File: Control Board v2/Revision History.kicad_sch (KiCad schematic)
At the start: 0 parts

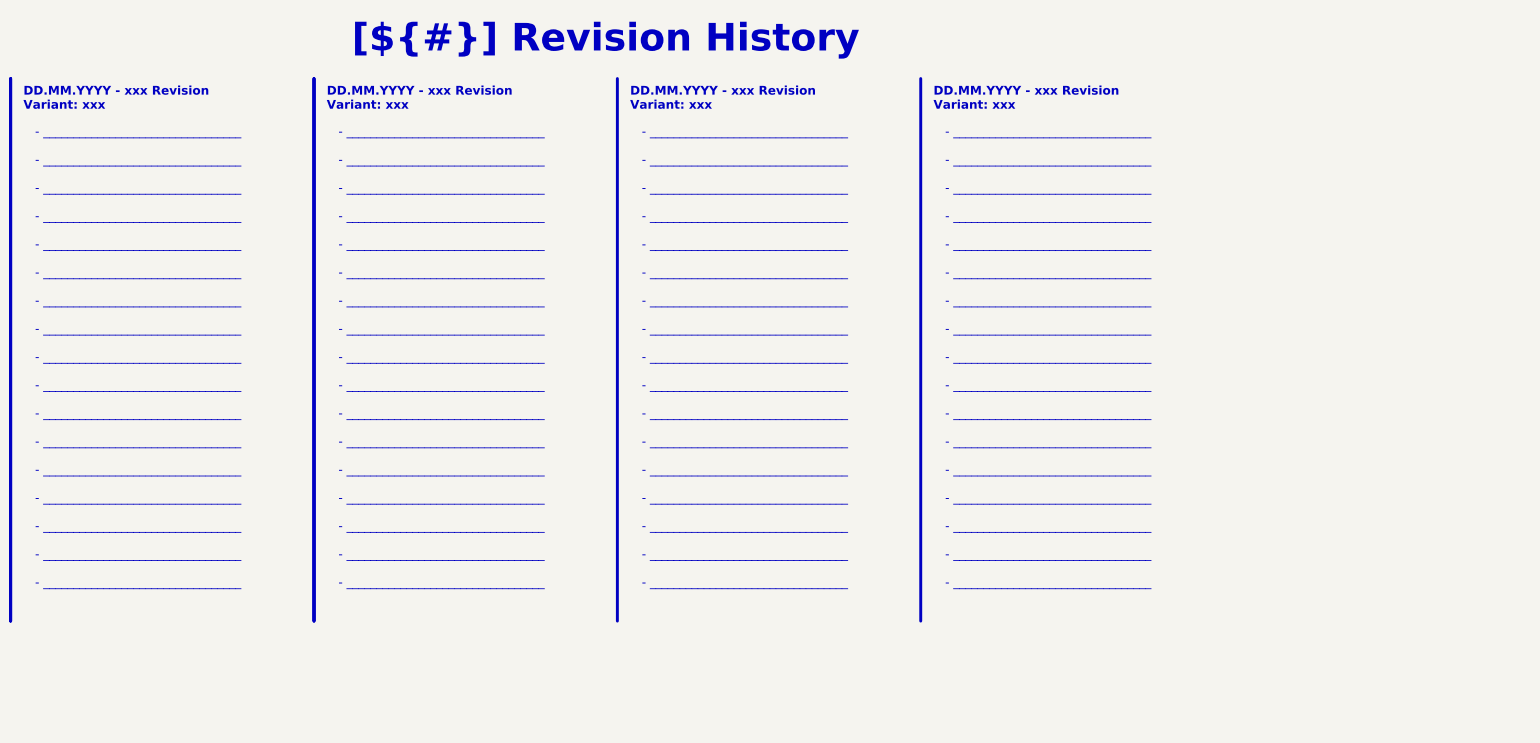
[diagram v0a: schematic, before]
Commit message: Finish preparing the template for v2 design
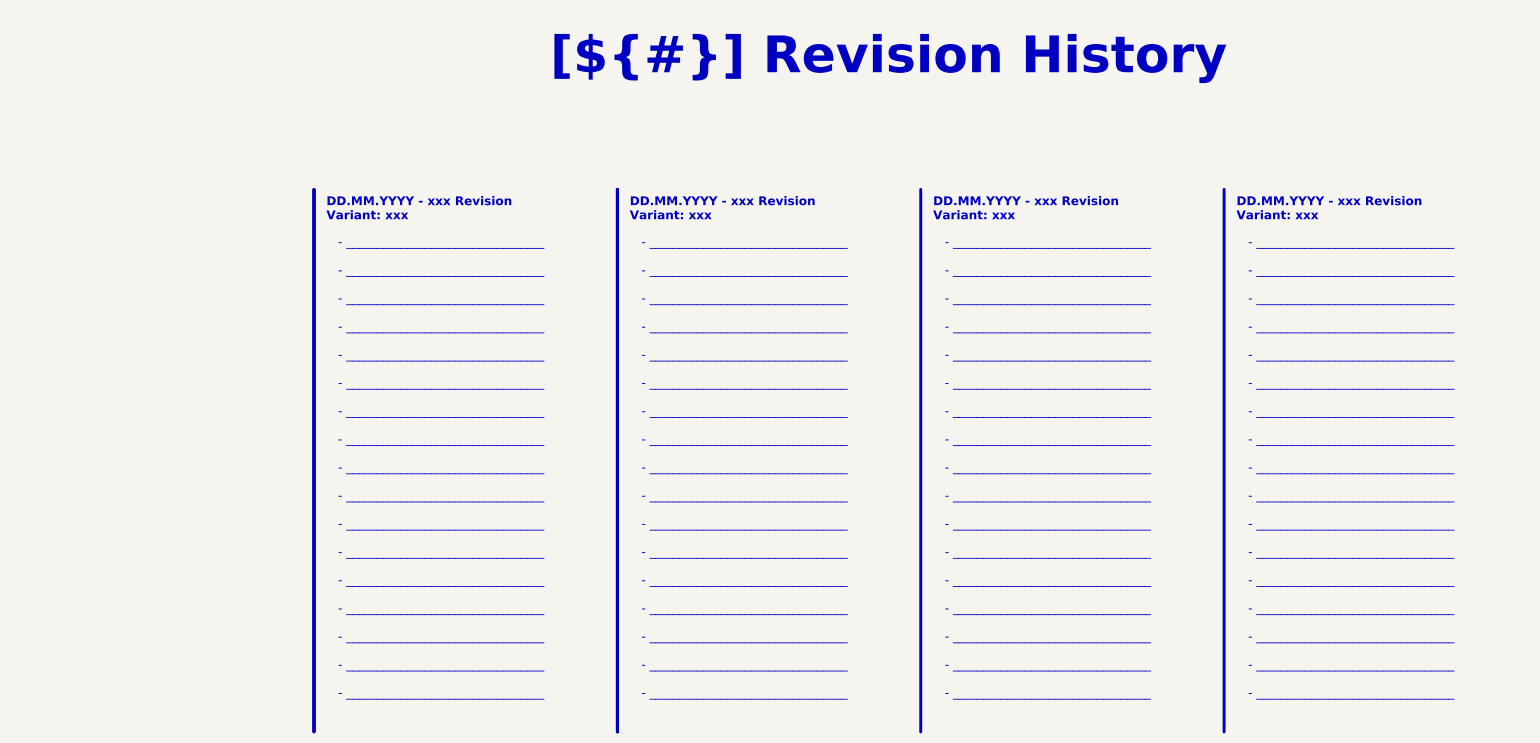
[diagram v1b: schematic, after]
